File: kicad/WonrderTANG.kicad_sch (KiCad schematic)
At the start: 31 parts, among them CON1 MSX-CONNECTOR, J1 Conn_02x01, J2 AudioJack3, J3 Conn_02x01, Q1 2N3904, U1 SN74LVC245AN, U2 SN74LVC245AN, U3 SN74LVC245AN, U4 SN74LVC245AN, U5 Tang_Nano_20k, U6 SN74LVC245AN

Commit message: version d schematic
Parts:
- added Q2: 2N3904, Package_TO_SOT_THT:TO-92_Inline, symbol Transistor_BJT:2N3904
- added R6: 2.2K, Resistor_THT:R_Axial_DIN0207_L6.3mm_D2.5mm_P10.16mm_Horizontal, symbol Device:R
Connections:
- net GND: now also Q2.1 (E)
- net INT: now also Q2.3 (C); no longer U2.18 (B0)
- new net: Q2.2 (B), R6.2
- new net INT_SW: R6.1, U2.18 (B0)

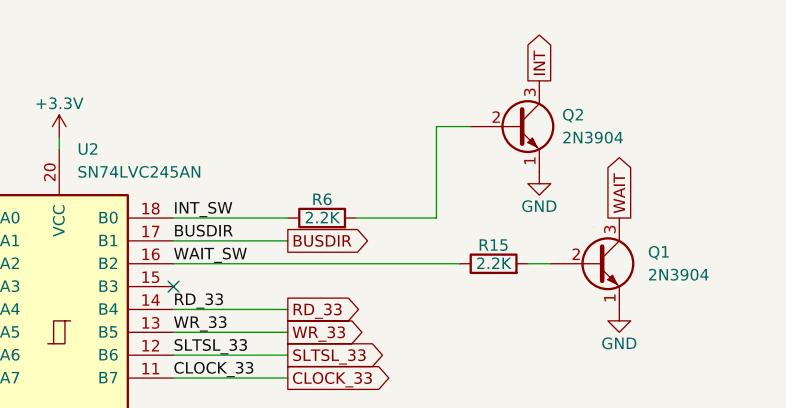
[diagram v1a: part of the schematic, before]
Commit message: Revert "version d schematic"
This reverts commit 586f92a0309d7defb717df5fd5272d4bcb2072a4.
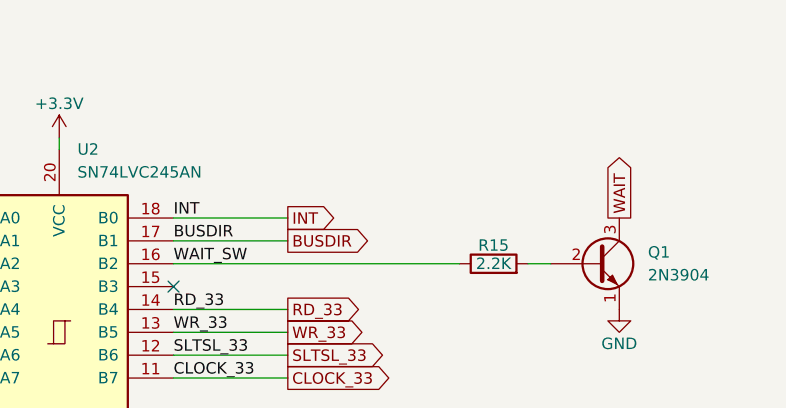
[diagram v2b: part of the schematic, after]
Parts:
- removed Q2: 2N3904, Package_TO_SOT_THT:TO-92_Inline, symbol Transistor_BJT:2N3904
- removed R6: 2.2K, Resistor_THT:R_Axial_DIN0207_L6.3mm_D2.5mm_P10.16mm_Horizontal, symbol Device:R
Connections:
- net INT_SW is gone; now on net INT: U2.18 (B0)

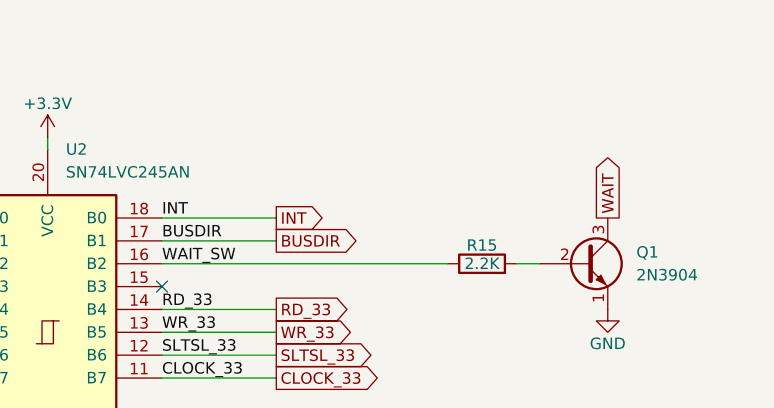
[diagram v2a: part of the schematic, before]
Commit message: New PCB Version 1.0.2d
A new firmware inverting the INT outpult needs to be submitted.
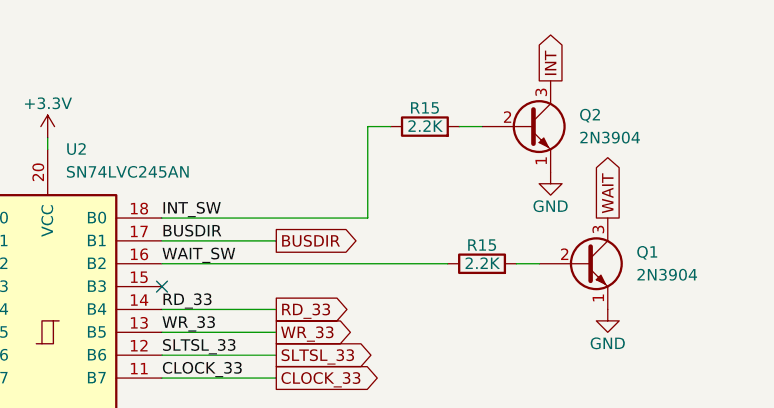
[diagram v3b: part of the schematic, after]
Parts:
- added Q2: 2N3904, Package_TO_SOT_THT:TO-92_Inline, symbol Transistor_BJT:2N3904
- added R15: 2.2K, Resistor_THT:R_Axial_DIN0207_L6.3mm_D2.5mm_P10.16mm_Horizontal, symbol Device:R
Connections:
- net GND: now also Q2.1 (E)
- net INT: now also Q2.3 (C); no longer U2.18 (B0)
- new net: Q2.2 (B), R15.2
- new net INT_SW: R15.1, U2.18 (B0)
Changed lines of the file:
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@@
     (stroke (width 0) (type default))
   )
-  (wire (pts (xy 325.12 48.26) (xy 337.82 48.26))
+  (wire (pts (xy 325.12 48.26) (xy 347.98 48.26))
     (stroke (width 0) (type default))
   )
@@
     (stroke (width 0) (type default))
   )
+  (wire (pts (xy 347.98 38.1) (xy 350.52 38.1))
+    (stroke (width 0) (type default))
+  )
   (wire (pts (xy 273.685 53.34) (xy 279.4 53.34))
     (stroke (width 0) (type default))
@@
     (stroke (width 0) (type default))
   )
+  (wire (pts (xy 347.98 48.26) (xy 347.98 38.1))
+    (stroke (width 0) (type default))
+  )
   (wire (pts (xy 149.86 99.06) (xy 152.4 99.06))
     (stroke (width 0) (type default))
@@
     (stroke (width 0) (type default))
   )
+  (wire (pts (xy 358.14 38.1) (xy 360.68 38.1))
+    (stroke (width 0) (type default))
+  )
   (wire (pts (xy 337.82 138.43) (xy 340.36 138.43))
     (stroke (width 0) (type default))
@@
     (effects (font (size 1.27 1.27)) (justify left bottom))
   )
-  (label "INT" (at 325.12 48.26 0) (fields_autoplaced)
+  (label "INT_SW" (at 325.12 48.26 0) (fields_autoplaced)
     (effects (font (size 1.27 1.27)) (justify left bottom))
   )
@@
     )
   )
-  (global_label "INT" (shape output) (at 337.82 48.26 0) (fields_autoplaced)
+  (global_label "INT" (shape output) (at 368.3 33.02 90) (fields_autoplaced)
     (effects (font (size 1.27 1.27)) (justify left))
-    (property "Intersheetrefs" "${INTERSHEET_REFS}" (at 342.9745 48.26 0)
+    (property "Intersheetrefs" "${INTERSHEET_REFS}" (at 368.3 27.7861 90)
       (effects (font (size 1.27 1.27)) (justify left) hide)
     )
@@
     )
   )
+  (symbol (lib_id "power:GND") (at 368.3 43.18 0) (unit 1)
+    (in_bom yes) (on_board yes) (dnp no)
+    (property "Reference" "#PWR091" (at 368.3 49.53 0)
+      (effects (font (size 1.27 1.27)) hide)
+    )
+    (property "Value" "GND" (at 368.3 46.99 0)
+      (effects (font (size 1.27 1.27)))
+    )
+    (property "Footprint" "" (at 368.3 43.18 0)
+      (effects (font (size 1.27 1.27)) hide)
+    )
+    (property "Datasheet" "" (at 368.3 43.18 0)
+      (effects (font (size 1.27 1.27)) hide)
+    )
+    (pin "1")
+    (instances
+      (project "Omega-Mainboard"
+        (path "/494667ff-8681-4396-86d5-0cbe152842af/00000000-0000-0000-0000-00005bf99f40"
+          (reference "#PWR091") (unit 1)
+        )
+      )
+      (project "WonrderTANG"
+        (path "/aac9604b-8c84-42de-bd09-e07036aaaac8"
+          (reference "#PWR048") (unit 1)
+        )
+      )
+    )
+  )
   (symbol (lib_id "Device:R") (at 331.47 138.43 90) (unit 1)
     (in_bom yes) (on_board yes) (dnp no)
@@
     )
   )
+  (symbol (lib_id "Device:R") (at 354.33 38.1 90) (unit 1)
+    (in_bom yes) (on_board yes) (dnp no)
+    (property "Reference" "R15" (at 354.33 36.068 90)
+      (effects (font (size 1.27 1.27)))
+    )
+    (property "Value" "2.2K" (at 354.33 38.1 90)
+      (effects (font (size 1.27 1.27)))
+    )
+    (property "Footprint" "Resistor_THT:R_Axial_DIN0207_L6.3mm_D2.5mm_P10.16mm_Horizontal" (at 354.33 39.878 90)
+      (effects (font (size 1.27 1.27)) hide)
+    )
+    (property "Datasheet" "" (at 354.33 38.1 0)
+      (effects (font (size 1.27 1.27)) hide)
+    )
+    (pin "1")
+    (pin "2")
+    (instances
+      (project "Omega-Mainboard"
+        (path "/494667ff-8681-4396-86d5-0cbe152842af/00000000-0000-0000-0000-00005bf99f40"
+          (reference "R15") (unit 1)
+        )
+      )
+      (project "WonrderTANG"
+        (path "/aac9604b-8c84-42de-bd09-e07036aaaac8"
+          (reference "R6") (unit 1)
+        )
+      )
+    )
+  )
   (symbol (lib_id "power:GND") (at 99.06 184.15 0) (unit 1)
     (in_bom yes) (on_board yes) (dnp no) (fields_autoplaced)
@@
         )
       )
+    )
+  )
+  (symbol (lib_id "Transistor_BJT:2N3904") (at 365.76 38.1 0) (unit 1)
+    (in_bom yes) (on_board yes) (dnp no) (fields_autoplaced)
+    (property "Reference" "Q2" (at 371.475 36.83 0)
+      (effects (font (size 1.27 1.27)) (justify left))
+    )
+    (property "Value" "2N3904" (at 371.475 39.37 0)
+      (effects (font (size 1.27 1.27)) (justify left))
+    )
+    (property "Footprint" "Package_TO_SOT_THT:TO-92_Inline" (at 370.84 40.005 0)
+      (effects (font (size 1.27 1.27) italic) (justify left) hide)
+    )
+    (property "Datasheet" "https://www.onsemi.com/pub/Collateral/2N3903-D.PDF" (at 365.76 38.1 0)
+      (effects (font (size 1.27 1.27)) (justify left) hide)
+    )
+    (pin "1")
+    (pin "2")
+    (pin "3")
+    (instances
+      (project "WonrderTANG"
+        (path "/aac9604b-8c84-42de-bd09-e07036aaaac8"
+          (reference "Q2") (unit 1)
+        )
+      )

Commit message: version 2.0b
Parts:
- removed C57 (x2): 105, Capacitor_THT:C_Disc_D5.0mm_W2.5mm_P2.50mm, symbol Device:C
- removed C76 (x2): 10uF, Capacitor_THT:CP_Radial_D5.0mm_P2.00mm, symbol Omega-Mainboard-rescue:CP1-Device
- removed J1: Conn_02x01, Connector_PinHeader_2.54mm:PinHeader_2x01_P2.54mm_Vertical, symbol Connector_Generic:Conn_02x01
- removed R15: 330, Resistor_THT:R_Axial_DIN0207_L6.3mm_D2.5mm_P10.16mm_Horizontal, symbol Device:R
- removed R41 (x2): 47, Resistor_THT:R_Axial_DIN0207_L6.3mm_D2.5mm_P10.16mm_Horizontal, symbol Device:R
- added C1, C2: 4.7u, Capacitor_THT:CP_Radial_D5.0mm_P2.50mm, symbol Device:C_Polarized
- added R1: 330, Resistor_THT:R_Axial_DIN0207_L6.3mm_D2.5mm_P10.16mm_Horizontal, symbol Device:R
- CON1: footprint Mis_huellas:CARTRIDGE_MSX -> Tang20K:CARTRIDGE_MSX_NOCUT
- J2: footprint Connector_Audio:Jack_3.5mm_CUI_SJ1-3533NG_Horizontal -> Tang20K:SJ1-3523N
- Q1, Q2: footprint Package_TO_SOT_THT:TO-92_Inline -> Package_TO_SOT_THT:TO-92_Inline_Wide
- U5: footprint Mis_huellas:Tang_Nano_20k -> Tang20K:Tang_Nano_20k_Audio; symbol Mi_libreria:Tang_Nano_20k -> Tang20K:Tang_Nano_20k_Audio
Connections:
- net AUDIO_33 is gone; now on net D1_33: U5.35 (41_IOB43A)
- net JP is gone; now on net D6_33: U5.22 (53_IOR38B)
- net SOUND_33 is gone; now on net D7_33: U5.29 (49_IOR49A)
- net D1_33: no longer U5.34 (56_IOR36A)
- net D2_33: now also U5.28 (86_IOT4A); no longer U5.33 (54_IOR38A)
- net D6_33: no longer U5.32 (51_IOR45A)
- net D7_33: no longer U5.30 (55_IOR36B)
- net LED: now also U5.3 (75_IOT34A), R1.1; no longer U5.28 (86_IOT4A)
- net SOUNDIN: now also C1.2; no longer J3.2 (Pin_2)
- net at J2.R, J2.T: now also C2.2
- net at D1.2 (A): now also R1.2
- net at J3.1 (Pin_1): now also C1.1
- new net: C2.1, J3.2 (Pin_2)
- no-connect marks 9 -> 8
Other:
- title: MSX-Tang Nano 9K Breakout -> MSX wonderTANG 2.0
- moved on the sheet: C10, C11, C12, C5, C6, C7, C76, C8, C9, CON1, D2, J2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

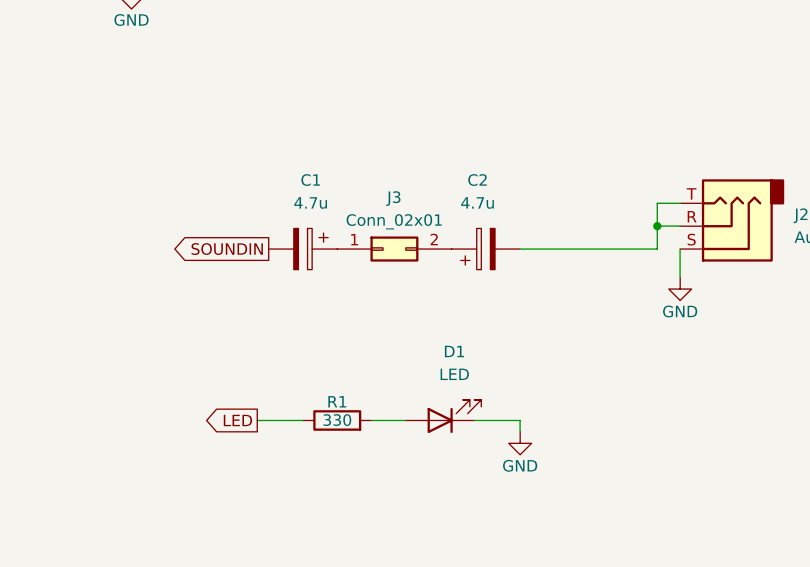
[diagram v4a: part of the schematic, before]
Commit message: kicad: sync schematic labels with pcb
Signed-off-by: Albert Herranz <albert_herranz@yahoo.es>
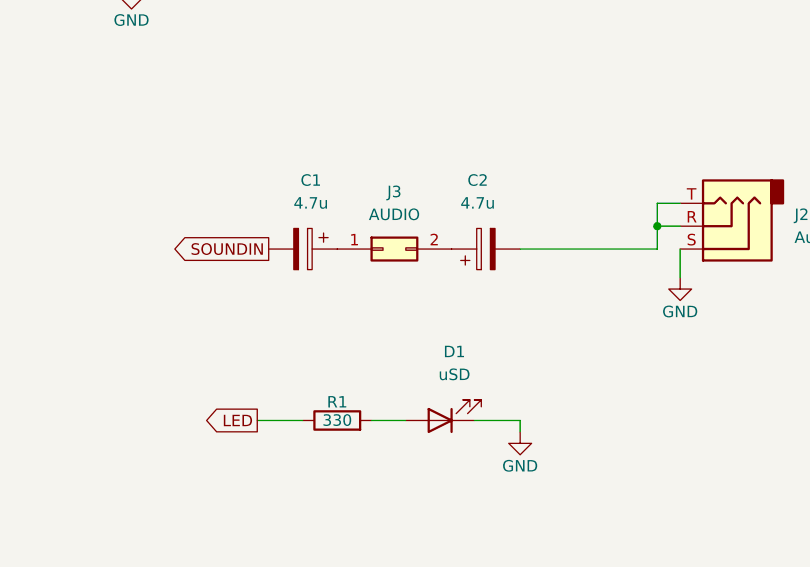
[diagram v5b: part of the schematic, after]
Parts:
- D1: value LED -> uSD
- J3: value Conn_02x01 -> AUDIO
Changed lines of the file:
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@@
 			)
 		)
-		(property "Value" "LED"
+		(property "Value" "uSD"
 			(at 350.8375 124.46 0)
 			(effects
@@
 		(fields_autoplaced yes)
 		(property "Reference" "J3"
-			(at 344.17 104.775 0)
-			(effects
-				(font
-					(size 1.27 1.27)
-				)
-			)
-		)
-		(property "Value" "Conn_02x01"
-			(at 344.17 107.315 0)
-			(effects
-				(font
+			(at 344.17 104.14 0)
+			(effects
+				(font
+					(size 1.27 1.27)
+				)
+			)
+		)
+		(property "Value" "AUDIO"
+			(at 344.17 106.68 0)
+			(effects
+				(font

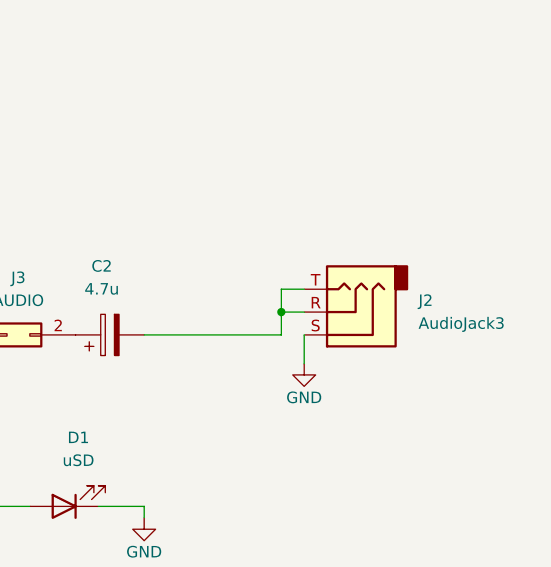
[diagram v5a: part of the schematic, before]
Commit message: kicad: change audio connector from CP1-3523N to SJ1-3525N
Signed-off-by: Albert Herranz <albert_herranz@yahoo.es>
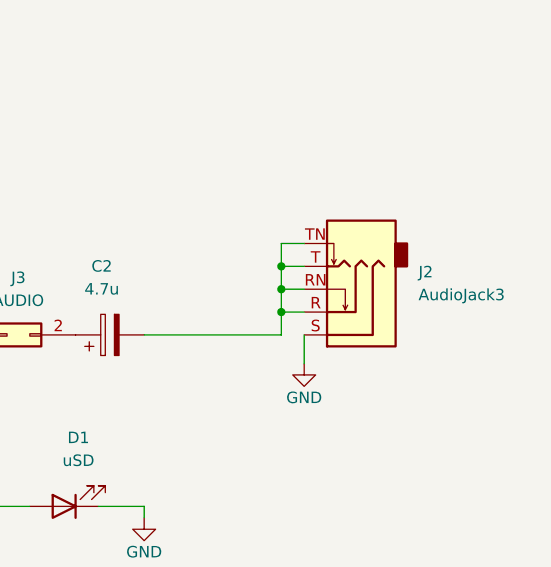
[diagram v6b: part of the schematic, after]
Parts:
- J2: footprint Tang20K:SJ1-3523N -> Connector_Audio:Jack_3.5mm_CUI_SJ1-3525N_Horizontal; symbol Connector_Audio:AudioJack3 -> Connector_Audio:AudioJack3_SwitchTR
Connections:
- net at C2.2, J2.R, J2.T: now also J2.RN, J2.TN
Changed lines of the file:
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@@
 		(color 0 0 0 0)
 	)
+	(junction
+		(at 373.38 105.41)
+		(diameter 0)
+		(color 0 0 0 0)
+	)
+	(junction
+		(at 373.38 102.87)
+		(diameter 0)
+		(color 0 0 0 0)
+	)
 	(no_connect
 		(at 327.66 55.88)
@@
 	(wire
 		(pts
+			(xy 375.92 102.87) (xy 373.38 102.87)
+		)
+		(stroke
+			(width 0)
+			(type default)
+		)
+	)
+	(wire
+		(pts
 			(xy 281.94 42.545) (xy 281.94 44.45)
 		)
@@
 	(wire
 		(pts
+			(xy 373.38 100.33) (xy 373.38 102.87)
+		)
+		(stroke
+			(width 0)
+			(type default)
+		)
+	)
+	(wire
+		(pts
 			(xy 201.93 227.33) (xy 204.47 227.33)
 		)
@@
 	(wire
 		(pts
+			(xy 375.92 100.33) (xy 373.38 100.33)
+		)
+		(stroke
+			(width 0)
+			(type default)
+		)
+	)
+	(wire
+		(pts
+			(xy 373.38 102.87) (xy 373.38 105.41)
+		)
+		(stroke
+			(width 0)
+			(type default)
+		)
+	)
+	(wire
+		(pts
 			(xy 229.87 109.22) (xy 242.57 109.22)
 		)
@@
 	)
 	(symbol
-		(lib_id "Connector_Audio:AudioJack3")
+		(lib_id "Connector_Audio:AudioJack3_SwitchTR")
 		(at 381 107.95 180)
 		(unit 1)
@@
 		(on_board yes)
 		(dnp no)
-		(fields_autoplaced yes)
 		(property "Reference" "J2"
-			(at 388.62 106.68 0)
+			(at 388.62 103.5049 0)
 			(effects
 				(font
@@
 		)
 		(property "Value" "AudioJack3"
-			(at 388.62 109.22 0)
+			(at 388.62 106.0449 0)
 			(effects
 				(font
@@
 			)
 		)
-		(property "Footprint" "Tang20K:SJ1-3523N"
+		(property "Footprint" "Connector_Audio:Jack_3.5mm_CUI_SJ1-3525N_Horizontal"
 			(at 381 107.95 0)
 			(effects
@@
 			)
 		)
-		(property "Description" ""
+		(property "Description" "Audio Jack, 3 Poles (Stereo / TRS), Switched TR Poles (Normalling)"
 			(at 381 107.95 0)
 			(effects
@@
 		(pin "T"
 		)
+		(pin "TN"
+		)
+		(pin "RN"
+		)
 		(instances
